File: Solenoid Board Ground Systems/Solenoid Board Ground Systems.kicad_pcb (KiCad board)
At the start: 2 copper layers, 63.5 x 25.4 mm, 32 parts, among them J1 OUT CHAN 1, J2 IN CHAN 1, J3 OUT CHAN 2, J4 IN CHAN 2

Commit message: Open
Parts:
- J1, J2, J3, J4: moved to B.Cu
- moved J3 22.6 mm to (57.5, 29.0), turned to 0 degrees
- moved D10 21.7 mm to (59.0, 34.9)
- moved R5 21.5 mm to (56.1, 36.3)
- moved D9 21.4 mm to (56.1, 33.1)
- moved J2 18.4 mm to (51.5, 40.8), turned to 180 degrees
- moved D2 18.3 mm to (36.1, 34.8)
- moved J1 18.1 mm to (34.1, 28.9), turned to 0 degrees
- moved R1 17.8 mm to (33.2, 36.3)
- moved D1 17.7 mm to (33.2, 33.1)
- moved D8 17.1 mm to (53.3, 34.8)
- moved R4 16.0 mm to (50.4, 36.3)
- moved D7 16.0 mm to (50.4, 33.1)
- moved J4 15.0 mm to (74.9, 40.9), turned to 180 degrees
- moved D16 13.2 mm to (76.0, 34.9)
- moved R8 12.8 mm to (73.2, 36.3)
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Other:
- board size 63.5 x 25.4 mm -> 58.4 x 19.1 mm

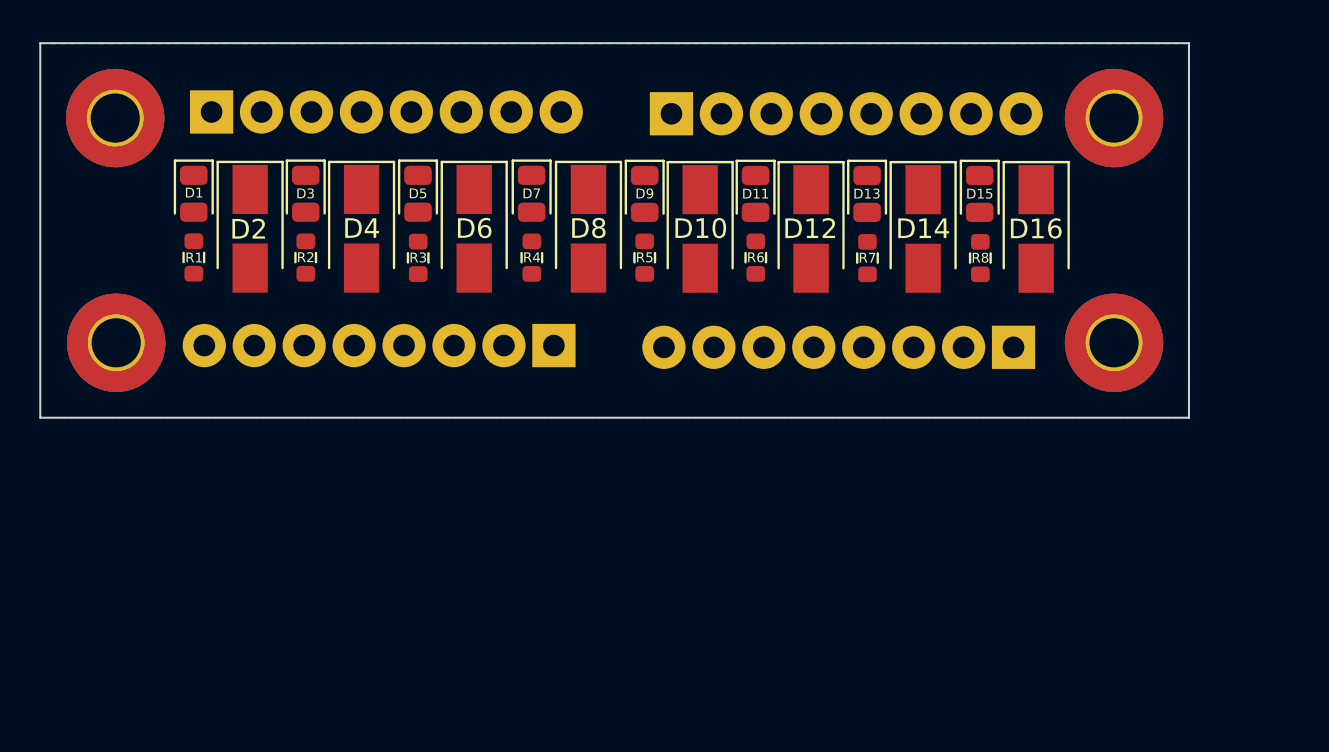
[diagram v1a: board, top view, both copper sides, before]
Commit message: Finished the Solenoid PCB
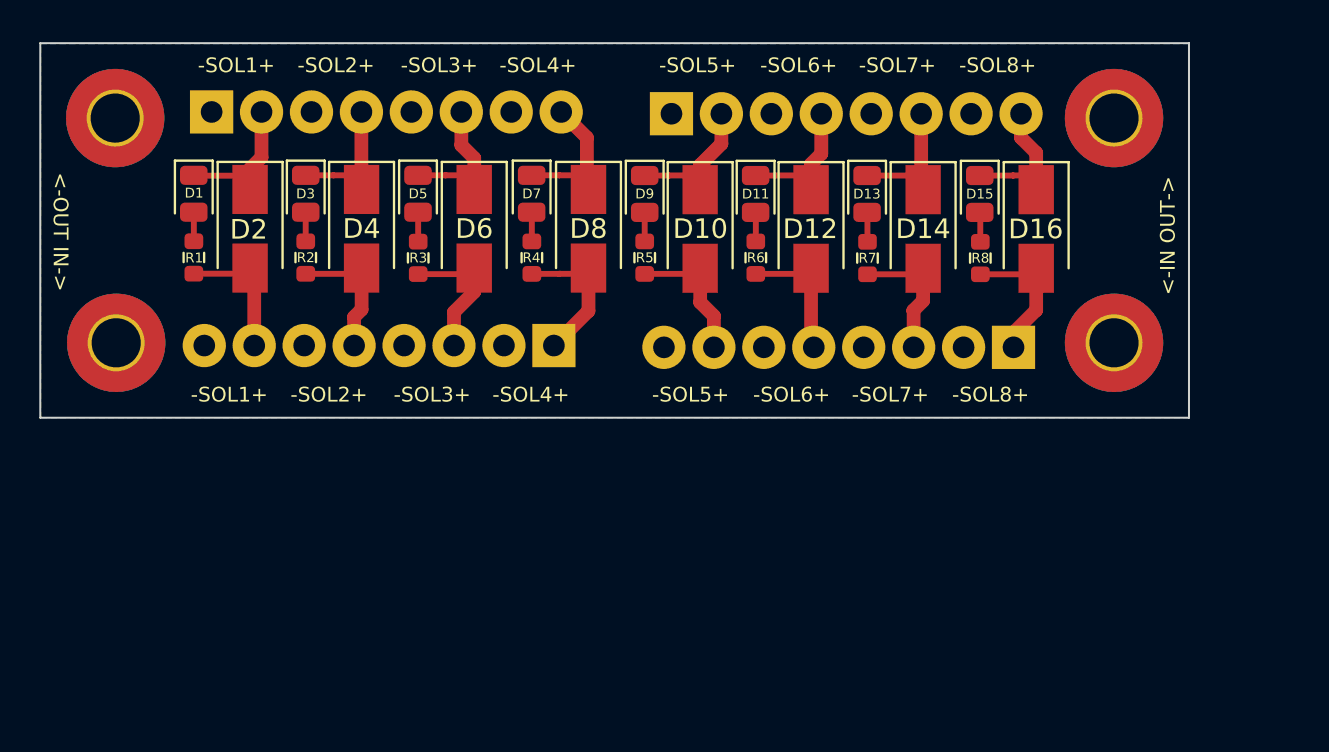
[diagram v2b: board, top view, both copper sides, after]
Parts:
- turned R4 to -90 degrees
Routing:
- net Net-(D7-Pad1): track 0.00 -> 7.70 mm
- net Net-(D8-Pad2): track 0.00 -> 7.67 mm
- net Net-(D16-Pad2): track 0.00 -> 7.46 mm
- net Net-(D10-Pad1): track 0.00 -> 7.43 mm
- net Net-(D5-Pad1): track 0.00 -> 7.37 mm
- net Net-(D15-Pad1): track 0.00 -> 7.35 mm
- net Net-(D6-Pad2): track 0.00 -> 7.34 mm
- net Net-(D1-Pad1): track 0.00 -> 7.34 mm
- net Net-(D10-Pad2): track 0.00 -> 7.25 mm
- net Net-(D11-Pad1): track 0.00 -> 7.19 mm
- net Net-(D14-Pad2): track 0.00 -> 7.19 mm
- net Net-(D3-Pad1): track 0.00 -> 7.08 mm
- net Net-(D4-Pad2): track 0.00 -> 7.06 mm
- net Net-(D13-Pad1): track 0.00 -> 7.05 mm
- net Net-(D12-Pad2): track 0.00 -> 7.01 mm
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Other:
- board text added: "-SOL1+"
- board text added: "-SOL2+"
- board text added: "-SOL3+"
- board text added: "-SOL4+"
- board text added: "-SOL5+"
- board text added: "-SOL6+"
- board text added: "-SOL7+"
- board text added: "-SOL8+"
- board text added: "<-IN OUT->"
- board text added: "<-OUT IN->"
- board text added: "AARHUS WUZ HERE"

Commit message: Lots of changes
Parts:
- removed J4: IN CHAN 2, TerminalBlock_Phoenix:TerminalBlock_Phoenix_MPT-0,5-8-2.54_1x08_P2.54mm_Horizontal
- H1, H2, H3, H4: footprint MountingHole:MountingHole_2.5mm_Pad_TopBottom -> MountingHole:MountingHole_3.2mm_M3_DIN965_Pad_TopBottom
- J1, J3: moved to F.Cu
- J2: value IN CHAN 1 -> CHAN IN; footprint TerminalBlock_Phoenix:TerminalBlock_Phoenix_MPT-0,5-8-2.54_1x08_P2.54mm_Horizontal -> TerminalBlock_Phoenix:TerminalBlock_Phoenix_MPT-0,5-9-2.54_1x09_P2.54mm_Horizontal; moved to F.Cu
- moved D15 42.2 mm to (31.1, 36.5)
- moved D16 42.2 mm to (34.0, 38.3)
- moved R8 42.2 mm to (31.1, 39.7)
- moved J1 40.8 mm to (74.8, 31.0), turned to 180 degrees
- moved R1 37.9 mm to (71.0, 39.8)
- moved D2 37.9 mm to (73.8, 38.3)
- moved D1 37.9 mm to (71.0, 36.5)
- moved D13 30.8 mm to (36.8, 36.5)
- moved D14 30.8 mm to (39.7, 38.3)
- moved R7 30.8 mm to (36.9, 39.7)
- moved R2 26.6 mm to (65.3, 39.8)
- moved D3 26.6 mm to (65.3, 36.5)
- moved D4 26.6 mm to (68.2, 38.3)
- moved D11 19.5 mm to (42.5, 36.5)
- moved D12 19.5 mm to (45.4, 38.3)
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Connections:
- J2 pad 1: Net-(D8-Pad2) -> Net-(D16-Pad2)
- J2 pad 2: GND -> Net-(D14-Pad2)
- J2 pad 3: Net-(D6-Pad2) -> Net-(D12-Pad2)
- J2 pad 4: GND -> Net-(D10-Pad2)
- J2 pad 5: Net-(D4-Pad2) -> Net-(D8-Pad2)
- J2 pad 6: GND -> Net-(D6-Pad2)
- J2 pad 7: Net-(D2-Pad2) -> Net-(D4-Pad2)
- J2 pad 8: GND -> Net-(D2-Pad2)
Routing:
- net Net-(D2-Pad2): track 7.01 -> 19.6 mm
- net Net-(D16-Pad2): track 7.46 -> 18.2 mm
- net Net-(D14-Pad2): track 7.19 -> 16.0 mm
- net Net-(D4-Pad2): track 7.06 -> 13.7 mm
- net Net-(D12-Pad2): track 7.01 -> 12.0 mm
- net Net-(D6-Pad2): track 7.34 -> 11.5 mm
- net Net-(D10-Pad2): track 7.25 -> 9.29 mm
- net Net-(D1-Pad1): track 7.34 -> 9.09 mm
- net Net-(D3-Pad1): track 7.08 -> 8.82 mm
- net Net-(D13-Pad1): track 7.05 -> 8.67 mm
- net Net-(D15-Pad1): track 7.35 -> 8.93 mm
- net Net-(D10-Pad1): track 7.43 -> 8.67 mm
- net Net-(D11-Pad1): track 7.19 -> 8.43 mm
- net Net-(D5-Pad1): track 7.37 -> 8.60 mm
- net Net-(D8-Pad2): track 7.67 -> 8.83 mm
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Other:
- board size 58.4 x 19.1 mm -> 58.4 x 25.4 mm
- board text added: "A OUT"
- board text added: "B OUT"
- board text added: "GND"
- board text added: "IN"
- board text added: "S1"
- board text added: "S2"
- board text added: "S3"
- board text added: "S4"
- board text added: "S5"
- board text added: "S6"
- board text added: "S7"
- board text added: "S8"

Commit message: Open multiple
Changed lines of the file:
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@@
   (segment (start 42.54 38.845) (end 42.54 37.4275) (width 0.3) (layer "F.Cu") (net 16))
   (segment (start 42.54 37.4275) (end 42.53 37.4175) (width 0.3) (layer "F.Cu") (net 16))
-  (segment (start 48.458237 42.638237) (end 46.07 42.638237) (width 1) (layer "F.Cu") (net 17))
-  (segment (start 45.35 41.918237) (end 45.35 40.26) (width 1) (layer "F.Cu") (net 17))
-  (segment (start 50.78 45.68) (end 50.78 44.96) (width 1) (layer "F.Cu") (net 17))
+  (segment (start 45.691763 42.26) (end 45.35 41.918237) (width 1) (layer "F.Cu") (net 17))
   (segment (start 42.54 40.495) (end 45.115 40.495) (width 0.3) (layer "F.Cu") (net 17))
   (segment (start 45.115 40.495) (end 45.35 40.26) (width 0.3) (layer "F.Cu") (net 17))
-  (segment (start 50.78 44.96) (end 48.458237 42.638237) (width 1) (layer "F.Cu") (net 17))
-  (segment (start 46.07 42.638237) (end 45.35 41.918237) (width 1) (layer "F.Cu") (net 17))
+  (segment (start 48.08 42.26) (end 45.691763 42.26) (width 1) (layer "F.Cu") (net 17))
+  (segment (start 50.78 45.68) (end 50.78 44.96) (width 1) (layer "F.Cu") (net 17))
+  (segment (start 50.78 44.96) (end 48.08 42.26) (width 1) (layer "F.Cu") (net 17))
+  (segment (start 45.35 41.918237) (end 45.35 40.26) (width 1) (layer "F.Cu") (net 17))
   (segment (start 40.23 33.53) (end 39.69 34.07) (width 0.8) (layer "F.Cu") (net 18))
   (segment (start 36.84 35.5425) (end 38.0525 35.5425) (width 0.3) (layer "F.Cu") (net 18))

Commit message: Ground System Work
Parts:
- J1: value OUT CHAN 1 -> OUT CHAN A
- J2: value CHAN IN -> POWER IN
- J3: value OUT CHAN 2 -> OUT CHAN B
- moved D2 8.15 mm to (81.7, 36.0), turned to 0 degrees
- moved D1 7.73 mm to (78.0, 39.6)
- moved R1 7.73 mm to (78.0, 42.9)
- moved D5 7.37 mm to (66.3, 39.7)
- moved R3 7.37 mm to (66.3, 43.0)
- moved D7 6.99 mm to (60.2, 39.6)
- moved R4 6.99 mm to (60.2, 42.9)
- moved D4 6.75 mm to (74.5, 36.0), turned to 0 degrees
- moved D3 6.48 mm to (70.9, 39.7)
- moved R2 6.48 mm to (70.9, 43.0)
- moved D13 6.33 mm to (42.3, 39.6)
- moved R7 6.33 mm to (42.4, 42.8)
- moved D9 5.87 mm to (53.1, 39.6)
- moved R5 5.87 mm to (53.1, 42.8)
- moved D15 5.47 mm to (35.5, 39.7)
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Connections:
- D1 pad 1: Net-(D1-Pad1) -> POW IN A
- D10 pad 1: Net-(D10-Pad1) -> POW IN E
- D10 pad 2: Net-(D10-Pad2) -> GND
- D11 pad 1: Net-(D11-Pad1) -> POW IN F
- D12 pad 1: Net-(D11-Pad1) -> POW IN F
- D12 pad 2: Net-(D12-Pad2) -> GND
- D13 pad 1: Net-(D13-Pad1) -> POW IN G
- D14 pad 1: Net-(D13-Pad1) -> POW IN G
- D14 pad 2: Net-(D14-Pad2) -> GND
- D15 pad 1: Net-(D15-Pad1) -> POW IN H
- D16 pad 1: Net-(D15-Pad1) -> POW IN H
- D16 pad 2: Net-(D16-Pad2) -> GND
- D2 pad 1: Net-(D1-Pad1) -> POW IN A
- D2 pad 2: Net-(D2-Pad2) -> GND
- D3 pad 1: Net-(D3-Pad1) -> POW IN B
- D4 pad 1: Net-(D3-Pad1) -> POW IN B
- D4 pad 2: Net-(D4-Pad2) -> GND
- D5 pad 1: Net-(D5-Pad1) -> POW IN C
- D6 pad 1: Net-(D5-Pad1) -> POW IN C
- D6 pad 2: Net-(D6-Pad2) -> GND
- D7 pad 1: Net-(D7-Pad1) -> POW IN D
- D8 pad 1: Net-(D7-Pad1) -> POW IN D
- D8 pad 2: Net-(D8-Pad2) -> GND
- D9 pad 1: Net-(D10-Pad1) -> POW IN E
- J1 pad 2: Net-(D1-Pad1) -> POW IN A
- J1 pad 4: Net-(D3-Pad1) -> POW IN B
- J1 pad 6: Net-(D5-Pad1) -> POW IN C
- J1 pad 8: Net-(D7-Pad1) -> POW IN D
- J2 pad 1: Net-(D16-Pad2) -> POW IN H
- J2 pad 2: Net-(D14-Pad2) -> POW IN G
- J2 pad 3: Net-(D12-Pad2) -> POW IN F
- J2 pad 4: Net-(D10-Pad2) -> POW IN E
- J2 pad 5: Net-(D8-Pad2) -> POW IN D
- J2 pad 6: Net-(D6-Pad2) -> POW IN C
- J2 pad 7: Net-(D4-Pad2) -> POW IN B
- J2 pad 8: Net-(D2-Pad2) -> POW IN A
- J3 pad 2: Net-(D10-Pad1) -> POW IN E
- J3 pad 4: Net-(D11-Pad1) -> POW IN F
- J3 pad 6: Net-(D13-Pad1) -> POW IN G
- J3 pad 8: Net-(D15-Pad1) -> POW IN H
- R1 pad 2: Net-(D2-Pad2) -> POW IN A
- R2 pad 2: Net-(D4-Pad2) -> POW IN B
- R3 pad 2: Net-(D6-Pad2) -> POW IN C
- R4 pad 2: Net-(D8-Pad2) -> POW IN D
- R5 pad 2: Net-(D10-Pad2) -> POW IN E
- R6 pad 2: Net-(D12-Pad2) -> POW IN F
- R7 pad 2: Net-(D14-Pad2) -> POW IN G
- R8 pad 2: Net-(D16-Pad2) -> POW IN H
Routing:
- net POW IN A: track 0.00 -> 44.8 mm
- net POW IN B: track 0.00 -> 36.5 mm
- net POW IN H: track 0.00 -> 36.0 mm
- net POW IN G: track 0.00 -> 30.7 mm
- net POW IN C: track 0.00 -> 29.7 mm
- net POW IN D: track 0.00 -> 28.5 mm
- net POW IN F: track 0.00 -> 27.4 mm
- net POW IN E: track 0.00 -> 27.1 mm
- net Net-(D2-Pad2): track 19.6 -> 0.00 mm
- net Net-(D16-Pad2): track 18.2 -> 0.00 mm
- net Net-(D14-Pad2): track 16.0 -> 0.00 mm
- net Net-(D4-Pad2): track 13.7 -> 0.00 mm
- net Net-(D12-Pad2): track 12.0 -> 0.00 mm
- net Net-(D6-Pad2): track 11.5 -> 0.00 mm
- net Net-(D10-Pad2): track 9.29 -> 0.00 mm
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- added copper zone on F.Cu, net GND
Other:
- board size 58.4 x 25.4 mm -> 63.5 x 30.5 mm

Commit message: AGS Board Work
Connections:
- D1 pad 1: POW IN A -> GND
- D11 pad 1: POW IN F -> GND
- D13 pad 1: POW IN G -> GND
- D15 pad 1: POW IN H -> GND
- D3 pad 1: POW IN B -> GND
- D5 pad 1: POW IN C -> GND
- D7 pad 1: POW IN D -> GND
- D9 pad 1: POW IN E -> GND
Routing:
- net POW IN E: track 27.1 -> 24.0 mm
- net POW IN D: track 28.5 -> 25.6 mm
- net POW IN A: track 44.8 -> 42.2 mm
- net POW IN B: track 36.5 -> 33.9 mm
- net POW IN F: track 27.4 -> 24.9 mm
- net POW IN H: track 36.0 -> 33.5 mm
- net POW IN G: track 30.7 -> 28.3 mm
- net POW IN C: track 29.7 -> 27.8 mm
- net GND: vias 16 -> 21

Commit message: Some Gerbs Some Work
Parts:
- D10, D12, D14, D16, D2, D4, D6, D8: footprint Diode_SMD:D_SMA -> Diode_THT:D_DO-41_SOD81_P2.54mm_Vertical_AnodeUp
- moved H2 11.4 mm to (29.2, 54.6)
- moved H4 11.4 mm to (85.1, 54.6)
- moved D1 4.35 mm to (75.4, 43.1)
- moved D5 4.14 mm to (63.9, 43.1)
- moved D7 4.04 mm to (58.2, 43.1)
- moved R6 4.04 mm to (49.1, 45.6), turned to 0 degrees
- moved D13 3.80 mm to (40.9, 43.1)
- moved D3 3.63 mm to (69.7, 43.1)
- moved D9 3.53 mm to (52.4, 43.1)
- moved D11 3.48 mm to (46.6, 43.1)
- moved D15 3.37 mm to (35.1, 43.1)
- moved R8 3.31 mm to (37.6, 45.6), turned to 0 degrees
- moved R5 3.25 mm to (54.9, 45.6), turned to 0 degrees
- moved J2 3.13 mm to (46.8, 53.2)
- moved R7 2.94 mm to (43.4, 45.6), turned to 0 degrees
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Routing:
- net POW IN A: track 42.2 -> 0.00 mm
- net POW IN B: track 33.9 -> 0.00 mm
- net POW IN H: track 33.5 -> 0.00 mm
- net POW IN G: track 28.3 -> 0.00 mm
- net POW IN C: track 27.8 -> 0.00 mm
- net POW IN D: track 25.6 -> 0.00 mm
- net POW IN F: track 24.9 -> 0.00 mm
- net POW IN E: track 24.0 -> 0.00 mm
- net Net-(D5-Pad2): track 1.57 -> 0.00 mm
- net Net-(D3-Pad2): track 1.54 -> 0.00 mm
- net Net-(D1-Pad2): track 1.53 -> 0.00 mm
- net Net-(D7-Pad2): track 1.52 -> 0.00 mm
- net Net-(D15-Pad2): track 1.51 -> 0.00 mm
- net Net-(D13-Pad2): track 1.48 -> 0.00 mm
- net Net-(D9-Pad2): track 1.44 -> 0.00 mm
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- removed copper zone on F.Cu, net GND
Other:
- board size 63.5 x 30.5 mm -> 63.5 x 33 mm

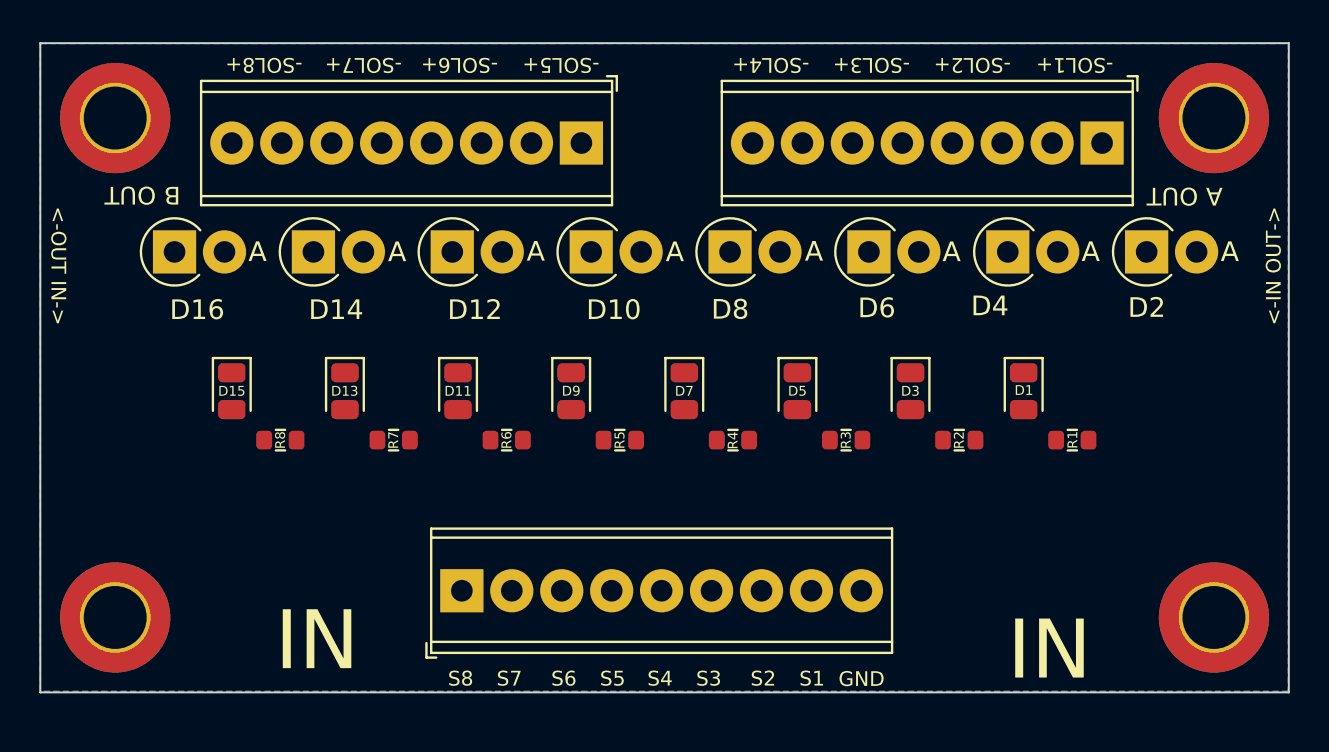
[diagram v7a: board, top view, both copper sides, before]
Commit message: Reworked the solenoid board
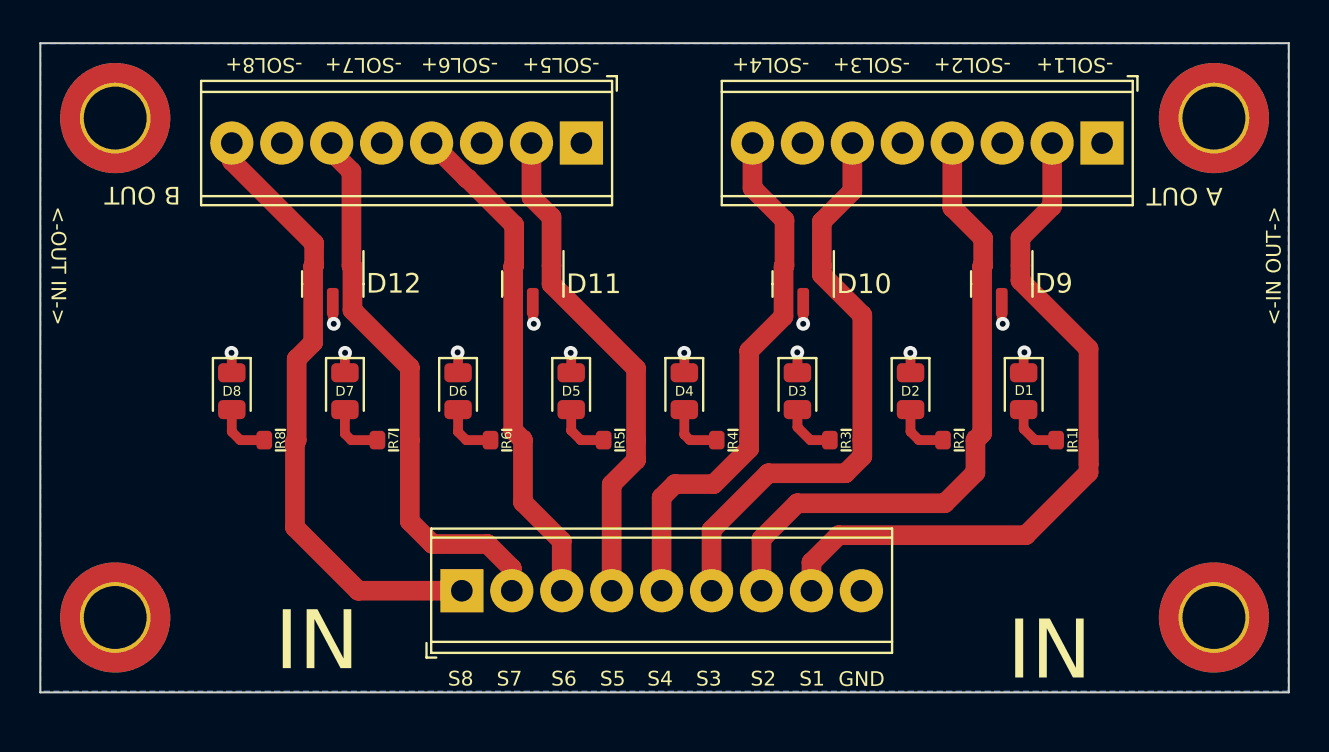
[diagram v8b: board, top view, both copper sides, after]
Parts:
- removed D14, D16: D_Small, Diode_THT:D_DO-41_SOD81_P2.54mm_Vertical_AnodeUp
- removed the D2 at (81.7, 36.0)
- removed the D4 at (74.6, 36.0)
- removed the D6 at (67.5, 36.0)
- removed the D8 at (60.5, 36.0)
- added D11: MMBZxx, Package_TO_SOT_SMD:SOT-23, F.Cu at (50.5, 37.6)
- added D9: MMBZxx, Package_TO_SOT_SMD:SOT-23, F.Cu at (74.3, 37.6)
- D10, D12: value D_Small -> MMBZxx; footprint Diode_THT:D_DO-41_SOD81_P2.54mm_Vertical_AnodeUp -> Package_TO_SOT_SMD:SOT-23
- moved D10 10.9 mm to (64.2, 37.6), turned to -90 degrees
- moved D12 6.29 mm to (40.3, 37.6), turned to -90 degrees
- renumbered D3 to D2, D5 to D3, D7 to D4, D9 to D5, D11 to D6, D13 to D7, D15 to D8
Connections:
- D10 pad 1: POW IN E -> POW IN C
- D10 pad 2: GND -> POW IN D
- D12 pad 1: POW IN F -> POW IN G
- D12 pad 2: GND -> POW IN H
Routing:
- net POW IN A: track 0.00 -> 37.5 mm
- net POW IN B: track 0.00 -> 32.5 mm
- net POW IN H: track 0.00 -> 31.5 mm
- net POW IN C: track 0.00 -> 29.7 mm
- net POW IN G: track 0.00 -> 28.2 mm
- net POW IN D: track 0.00 -> 27.2 mm
- net POW IN F: track 0.00 -> 25.6 mm
- net POW IN E: track 0.00 -> 25.5 mm
- net GND: track 0.00 -> 12.6 mm, vias 0 -> 12
- net Net-(D4-Pad2): track 0.00 -> 3.03 mm
- net Net-(D7-Pad2): track 0.00 -> 3.01 mm
- net Net-(D6-Pad2): track 0.00 -> 2.96 mm
- net Net-(D8-Pad2): track 0.00 -> 2.95 mm
- net Net-(D2-Pad2): track 0.00 -> 2.95 mm
- net Net-(D5-Pad2): track 0.00 -> 2.92 mm
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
